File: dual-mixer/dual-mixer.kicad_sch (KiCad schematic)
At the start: 29 parts, among them J1 Audio Output, J2 Audio Output, SW1 Merge/Split Gang 1, SW2 Merge/Split Gang 2, U1 TL072

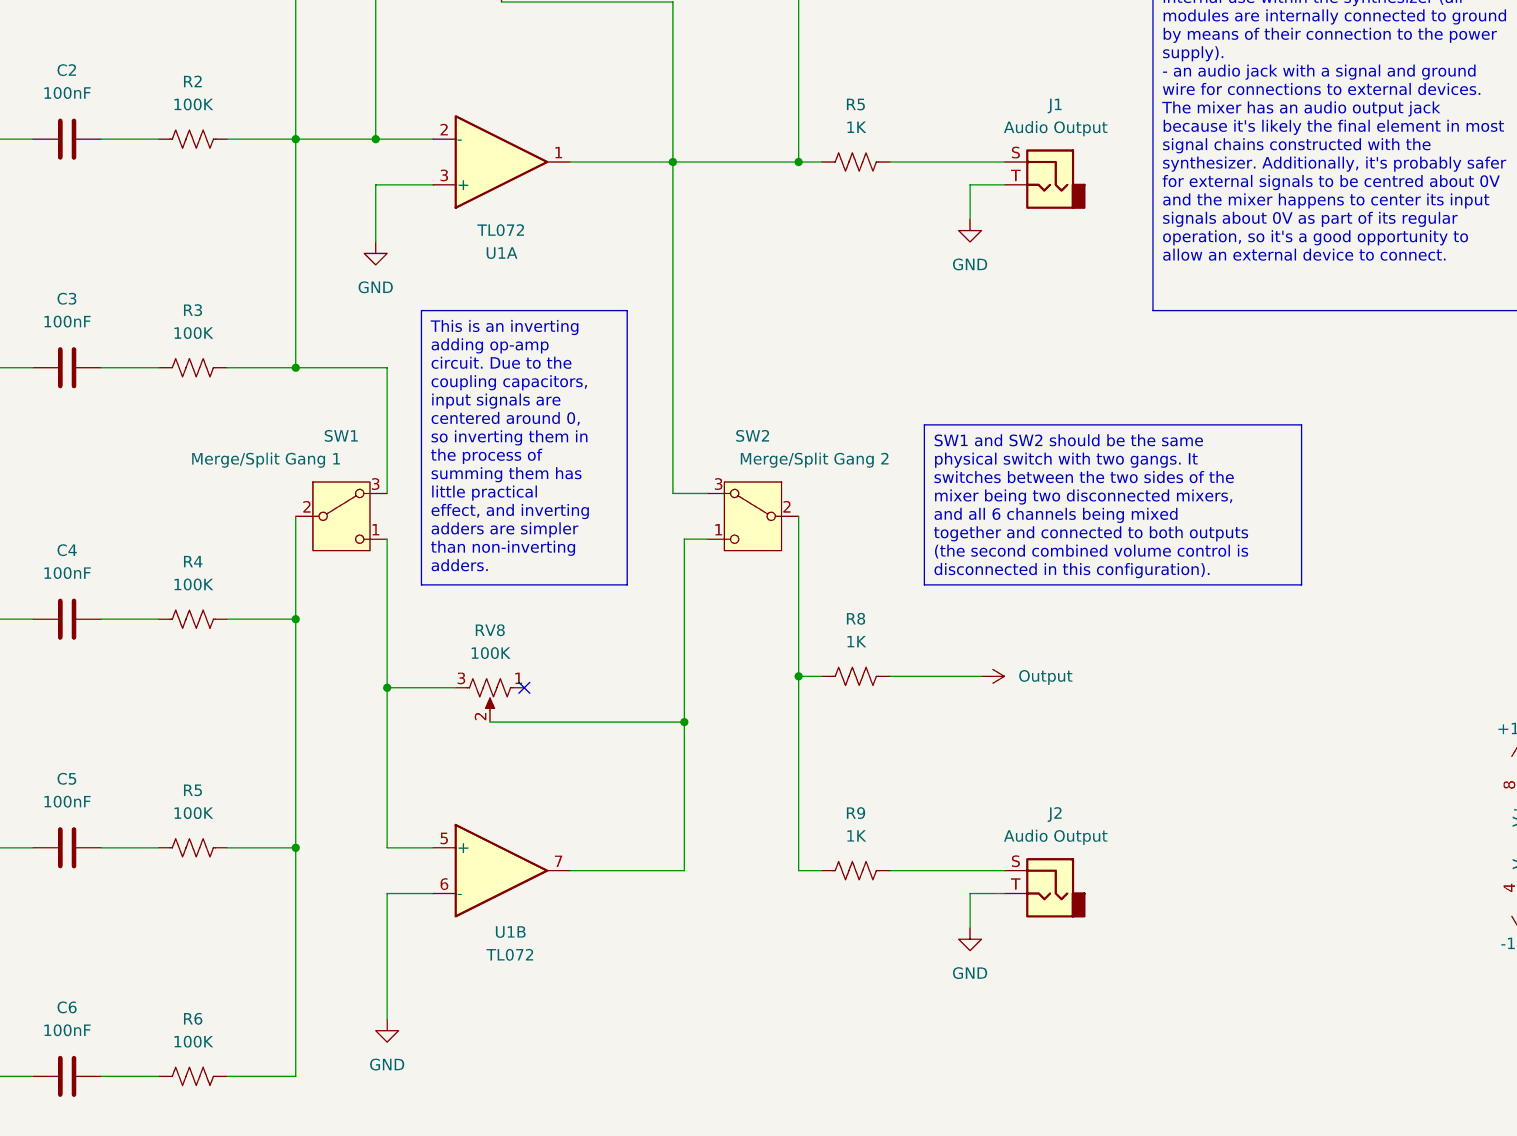
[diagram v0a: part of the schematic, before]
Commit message: Fixes for dual mixer
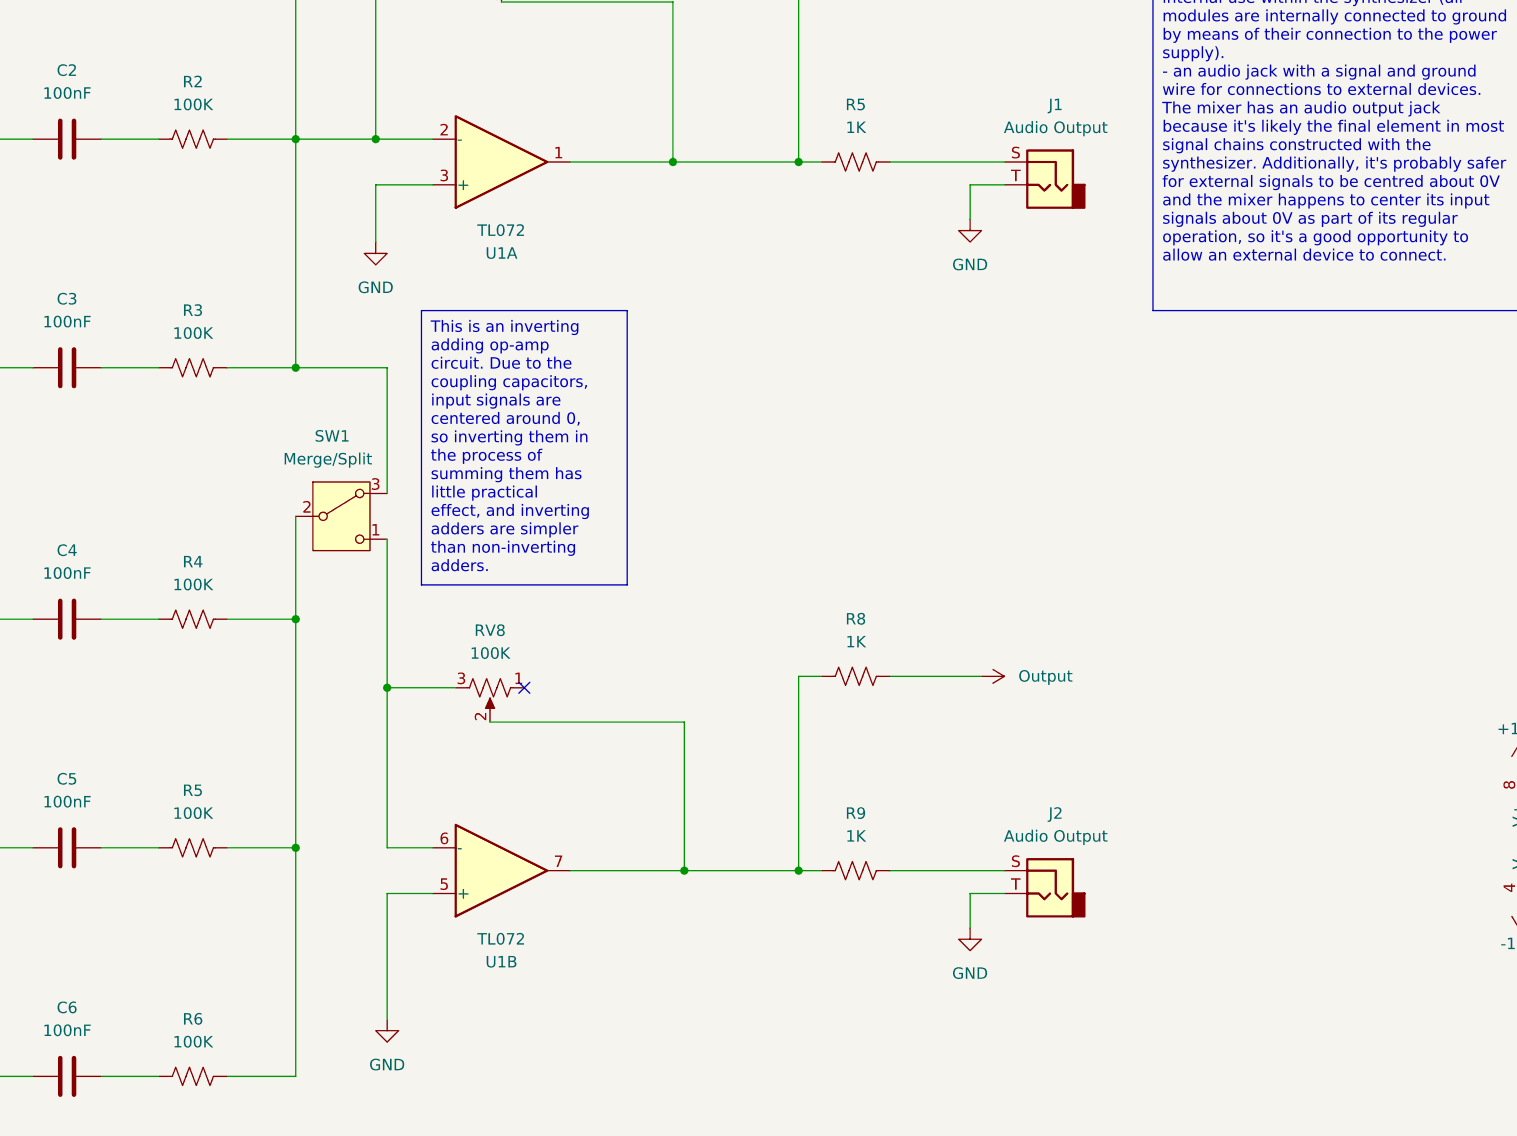
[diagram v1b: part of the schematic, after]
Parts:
- removed SW2: Merge/Split Gang 2, Button_Switch_SMD:Nidec_Copal_CAS-120A, symbol Switch:SW_Nidec_CAS-120A1
- SW1: value Merge/Split Gang 1 -> Merge/Split
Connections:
- net GND: now also U1.5 (+); no longer U1.6 (-)
- net at RV8.3, SW1.1 (C): now also U1.6 (-); no longer U1.5 (+)
- net at RV8.2, U1.7: now also R8.1, R9.1
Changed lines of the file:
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@@
 	(paper "A4")
 	(junction
-		(at 194.31 127)
+		(at 181.61 148.59)
 		(diameter 0)
 		(color 0 0 0 0)
 	)
 	(junction
-		(at 181.61 132.08)
+		(at 194.31 148.59)
 		(diameter 0)
 		(color 0 0 0 0)
@@
 	(wire
 		(pts
-			(xy 180.34 106.68) (xy 180.34 69.85)
-		)
-		(stroke
-			(width 0)
-			(type default)
-		)
-	)
-	(wire
-		(pts
 			(xy 104.14 67.31) (xy 109.22 67.31)
 		)
@@
 	(wire
 		(pts
-			(xy 181.61 111.76) (xy 181.61 132.08)
-		)
-		(stroke
-			(width 0)
-			(type default)
-		)
-	)
-	(wire
-		(pts
 			(xy 194.31 69.85) (xy 196.85 69.85)
 		)
@@
 	(wire
 		(pts
-			(xy 184.15 106.68) (xy 180.34 106.68)
-		)
-		(stroke
-			(width 0)
-			(type default)
-		)
-	)
-	(wire
-		(pts
 			(xy 138.43 171.45) (xy 130.81 171.45)
 		)
@@
 	(wire
 		(pts
-			(xy 161.29 52.07) (xy 180.34 52.07)
+			(xy 181.61 148.59) (xy 194.31 148.59)
 		)
 		(stroke
@@
 	(wire
 		(pts
-			(xy 90.17 139.7) (xy 100.33 139.7)
+			(xy 161.29 52.07) (xy 180.34 52.07)
 		)
 		(stroke
@@
 	(wire
 		(pts
-			(xy 157.48 48.26) (xy 147.32 48.26)
+			(xy 90.17 139.7) (xy 100.33 139.7)
 		)
 		(stroke
@@
 	(wire
 		(pts
-			(xy 100.33 60.96) (xy 100.33 63.5)
+			(xy 157.48 48.26) (xy 147.32 48.26)
 		)
 		(stroke
@@
 	(wire
 		(pts
-			(xy 194.31 109.22) (xy 194.31 127)
+			(xy 100.33 60.96) (xy 100.33 63.5)
 		)
 		(stroke
@@
 	(wire
 		(pts
-			(xy 181.61 111.76) (xy 184.15 111.76)
-		)
-		(stroke
-			(width 0)
-			(type default)
-		)
-	)
-	(wire
-		(pts
 			(xy 156.21 128.27) (xy 148.59 128.27)
 		)
@@
 		)
 	)
-	(text_box "SW1 and SW2 should be the same physical switch with two gangs. It switches between the two sides of the mixer being two disconnected mixers, and all 6 channels being mixed together and connected to both outputs (the second combined volume control is disconnected in this configuration)."
-		(exclude_from_sim no)
-		(at 208.28 99.06 0)
-		(size 41.91 17.78)
-		(stroke
-			(width 0)
-			(type default)
-		)
-		(fill
-			(type none)
-		)
-		(effects
-			(font
-				(size 1.27 1.27)
-			)
-			(justify left top)
-		)
-	)
 	(text_box "This is an inverting adding op-amp circuit. Due to the coupling capacitors, input signals are centered around 0, so inverting them in the process of summing them has little practical effect, and inverting adders are simpler than non-inverting adders."
 		(exclude_from_sim no)
@@
 		(dnp no)
 		(property "Reference" "SW1"
-			(at 143.51 100.33 0)
+			(at 142.494 100.33 0)
 			(effects
 				(font
@@
 			)
 		)
-		(property "Value" " Merge/Split Gang 1"
-			(at 135.128 102.87 0)
+		(property "Value" " Merge/Split"
+			(at 141.986 102.87 0)
 			(effects
 				(font
@@
 	)
 	(symbol
-		(lib_id "Switch:SW_Nidec_CAS-120A1")
-		(at 189.23 109.22 0)
-		(mirror y)
-		(unit 1)
-		(exclude_from_sim no)
-		(in_bom yes)
-		(on_board yes)
-		(dnp no)
-		(property "Reference" "SW2"
-			(at 189.23 100.33 0)
-			(effects
-				(font
-					(size 1.27 1.27)
-				)
-			)
-		)
-		(property "Value" " Merge/Split Gang 2"
-			(at 196.088 102.87 0)
-			(effects
-				(font
-					(size 1.27 1.27)
-				)
-			)
-		)
-		(property "Footprint" "Button_Switch_SMD:Nidec_Copal_CAS-120A"
-			(at 189.23 119.38 0)
-			(effects
-				(font
-					(size 1.27 1.27)
-				)
-				(hide yes)
-			)
-		)
-		(property "Datasheet" "https://www.nidec-components.com/e/catalog/switch/cas.pdf"
-			(at 189.23 116.84 0)
-			(effects
-				(font
-					(size 1.27 1.27)
-				)
-				(hide yes)
-			)
-		)
-		(property "Description" "Switch, single pole double throw"
-			(at 189.23 109.22 0)
-			(effects
-				(font
-					(size 1.27 1.27)
-				)
-				(hide yes)
-			)
-		)
-		(pin "1"
-		)
-		(pin "3"
-		)
-		(pin "2"
-		)
-		(instances
-			(project "dual-mixer"
-				(path "/75bbe09e-d3db-4deb-a3ee-e9cb8f5bc484"
-					(reference "SW2")
-					(unit 1)
-				)
-			)
-		)
-	)
-	(symbol
 		(lib_id "power:GND")
 		(at 148.59 165.1 0)
@@
 		(lib_id "Amplifier_Operational:TL072")
 		(at 161.29 148.59 0)
+		(mirror x)
 		(unit 2)
 		(exclude_from_sim no)
@@
 		(dnp no)
 		(property "Reference" "U1"
-			(at 162.306 155.448 0)
+			(at 161.29 158.75 0)
 			(effects
 				(font
@@
 		)
 		(property "Value" "TL072"
-			(at 162.306 157.988 0)
+			(at 161.29 156.21 0)
 			(effects
 				(font

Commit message: Update dual mixer
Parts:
- C1, C2, C3, C4, C5, C6: value 100nF -> 10uF
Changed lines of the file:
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@@
 			)
 		)
-		(property "Value" "100nF"
+		(property "Value" "10uF"
 			(at 113.03 36.83 90)
 			(effects
@@
 			)
 		)
-		(property "Value" "100nF"
+		(property "Value" "10uF"
 			(at 113.03 166.37 90)
 			(effects
@@
 			)
 		)
-		(property "Value" "100nF"
+		(property "Value" "10uF"
 			(at 113.03 62.23 90)
 			(effects
@@
 			)
 		)
-		(property "Value" "100nF"
+		(property "Value" "10uF"
 			(at 113.03 87.63 90)
 			(effects
@@
 			)
 		)
-		(property "Value" "100nF"
+		(property "Value" "10uF"
 			(at 113.03 115.57 90)
 			(effects
@@
 			)
 		)
-		(property "Value" "100nF"
+		(property "Value" "10uF"
 			(at 113.03 140.97 90)
 			(effects
